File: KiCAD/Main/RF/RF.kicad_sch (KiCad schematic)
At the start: 6 parts, among them J9 Conn_Coaxial

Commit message: Moved custom footprints into local KiCAD footprint library
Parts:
- U6: footprint E22-900T22S:E22-900T22S -> LRI:E22-900T22S
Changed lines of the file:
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@@
 			)
 		)
-		(property "Footprint" "E22-900T22S:E22-900T22S"
+		(property "Footprint" "LRI:E22-900T22S"
 			(at 176.53 109.22 0)
 			(effects

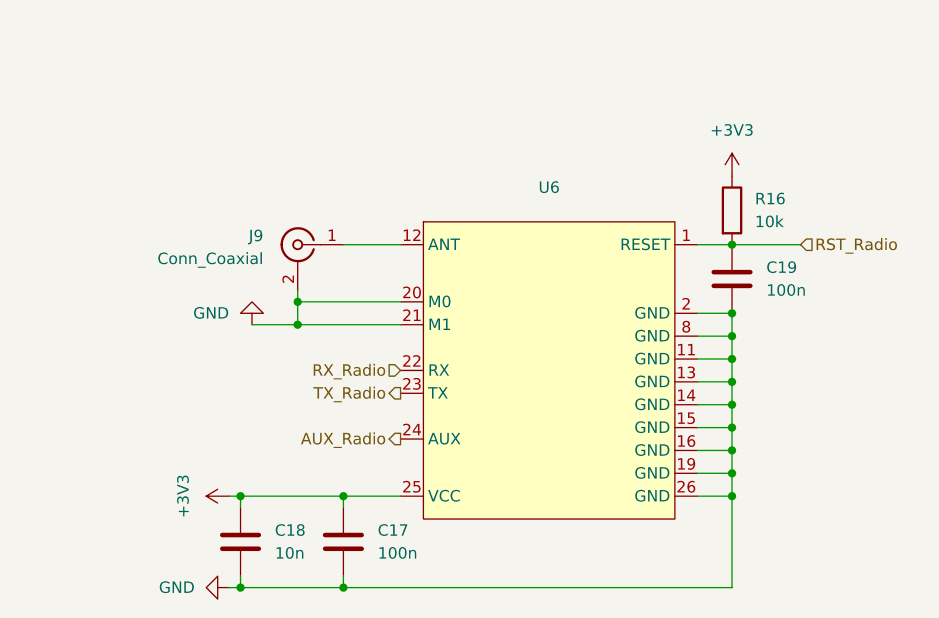
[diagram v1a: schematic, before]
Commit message: Update aux magnetometer, test THs, and silkscreens
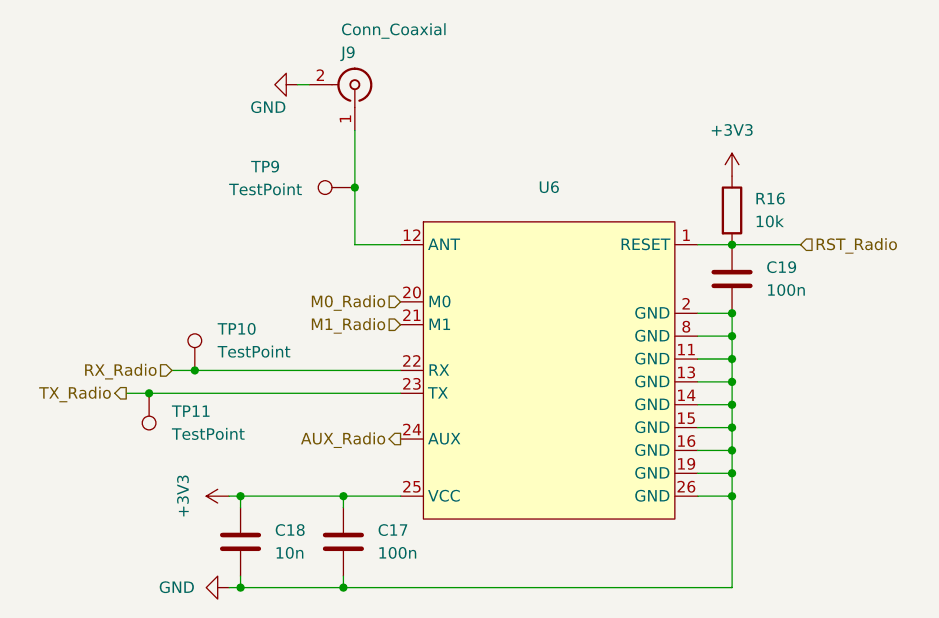
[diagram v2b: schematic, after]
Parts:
- added TP10, TP11, TP9: TestPoint, TestPoint:TestPoint_THTPad_1.5x1.5mm_Drill0.7mm, symbol Connector:TestPoint
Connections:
- net GND: no longer U6.20 (M0), U6.21 (M1)
- net RX_Radio: now also TP10.1
- net TX_Radio: now also TP11.1
- net at J9.1 (In), U6.12 (ANT): now also TP9.1
- new net M0_Radio: U6.20 (M0)
- new net M1_Radio: U6.21 (M1)
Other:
- moved on the sheet: J9

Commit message: Replace independent magnetometer, reformat test points, generate test gerber and BOM
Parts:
- TP10, TP11, TP9: footprint TestPoint:TestPoint_THTPad_1.5x1.5mm_Drill0.7mm -> TestPoint:TestPoint_Pad_D1.0mm
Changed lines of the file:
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@@
 			)
 		)
-		(property "Footprint" "TestPoint:TestPoint_THTPad_1.5x1.5mm_Drill0.7mm"
+		(property "Footprint" "TestPoint:TestPoint_Pad_D1.0mm"
 			(at 142.24 109.22 0)
 			(effects
@@
 			)
 		)
-		(property "Footprint" "TestPoint:TestPoint_THTPad_1.5x1.5mm_Drill0.7mm"
+		(property "Footprint" "TestPoint:TestPoint_Pad_D1.0mm"
 			(at 154.94 83.82 0)
 			(effects
@@
 			)
 		)
-		(property "Footprint" "TestPoint:TestPoint_THTPad_1.5x1.5mm_Drill0.7mm"
+		(property "Footprint" "TestPoint:TestPoint_Pad_D1.0mm"
 			(at 127 111.76 0)
 			(effects

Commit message: Update BOM and respective components according to LCSC supply, remove previously generated production files
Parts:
- TP10, TP11, TP9: now left out of the parts list
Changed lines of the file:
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@@
 		(unit 1)
 		(exclude_from_sim no)
-		(in_bom yes)
+		(in_bom no)
 		(on_board yes)
 		(dnp no)
@@
 		(unit 1)
 		(exclude_from_sim no)
-		(in_bom yes)
+		(in_bom no)
 		(on_board yes)
 		(dnp no)
@@
 		(unit 1)
 		(exclude_from_sim no)
-		(in_bom yes)
-		(on_board yes)
-		(dnp no)
+		(in_bom no)
+		(on_board yes)
+		(dnp no)

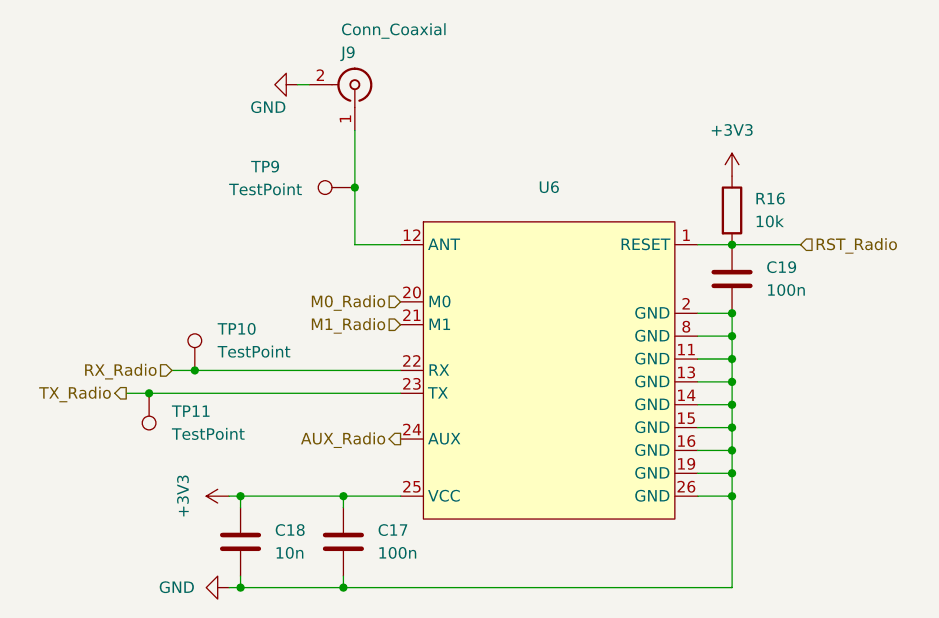
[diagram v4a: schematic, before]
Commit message: save after realizing branch was not switched to layoutv2
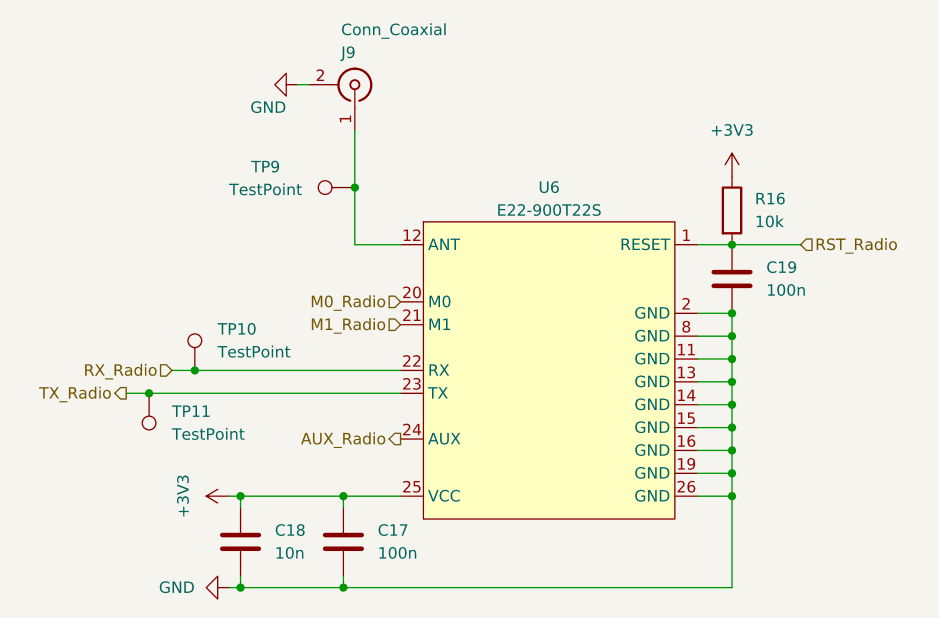
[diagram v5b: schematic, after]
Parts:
- U6: value ~ -> E22-900T22S
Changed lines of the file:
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@@
 			)
 		)
-		(property "Value" "~"
+		(property "Value" "E22-900T22S"
 			(at 176.53 91.44 0)
 			(effects
